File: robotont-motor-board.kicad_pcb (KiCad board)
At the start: 2 copper layers, 28 parts, among them J1 PWR_IN, J2 ENC, J3 MOTOR, J4 Conn_02x05_Odd_Even, U1 DMS3015SSS-13, U3 MIC5205-X.X

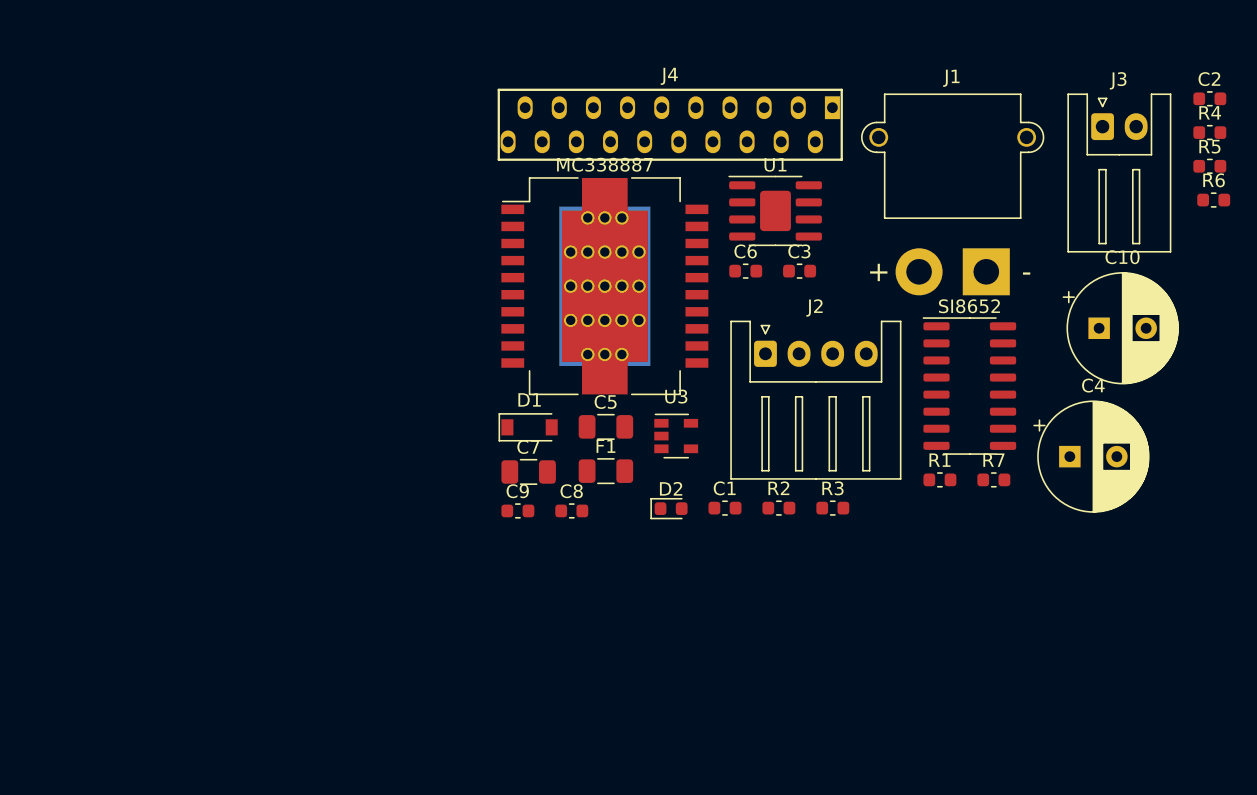
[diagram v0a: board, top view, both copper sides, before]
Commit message: v2.1 with jlcpcb components
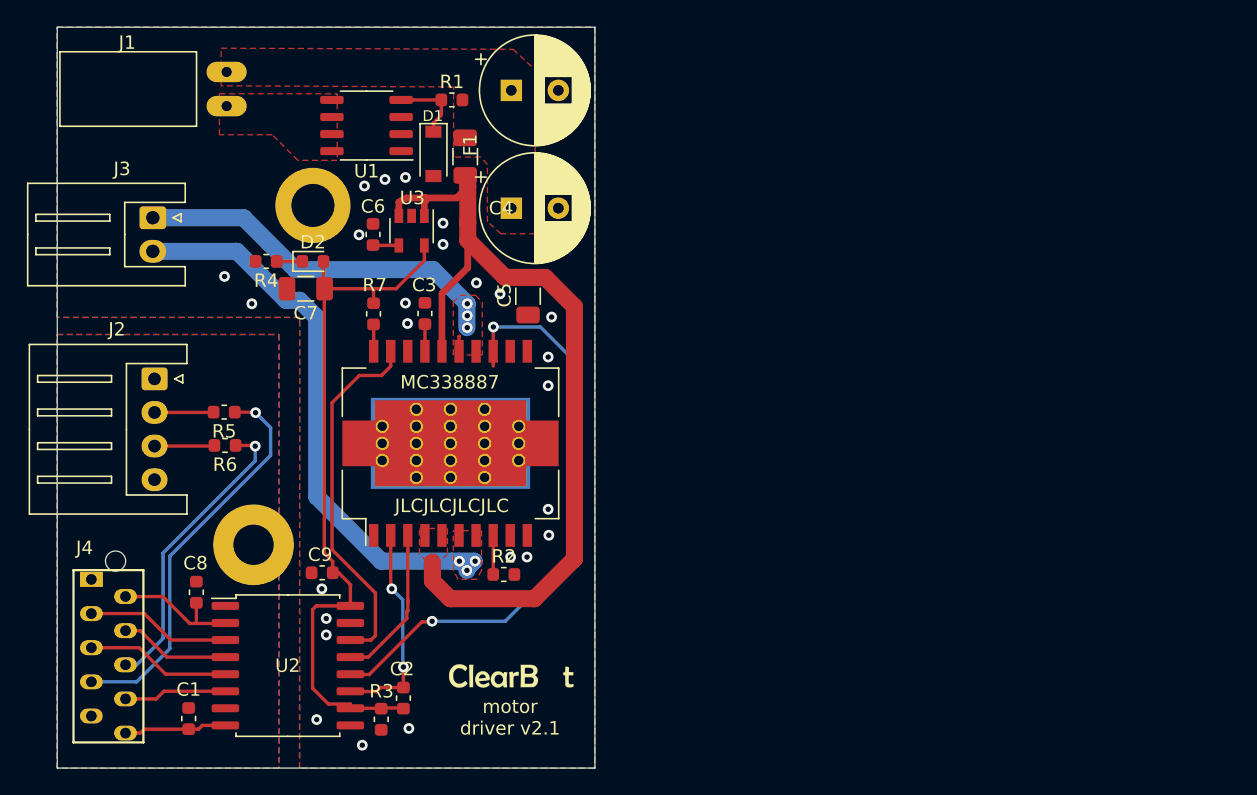
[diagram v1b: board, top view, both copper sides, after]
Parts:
- removed SI8652: SI8652-IS, Package_SO:SOIC-16_3.9x9.9mm_P1.27mm
- added G***: LOGO, robotont-motor-board:clearbot_logo, F.Cu at (134.4, 98.3)
- added H1: MountingHole_Pad, MountingHole:MountingHole_3mm_Pad, F.Cu at (115.2, 88.5)
- added H2: MountingHole_Pad, MountingHole:MountingHole_3.2mm_M3_DIN965_Pad, F.Cu at (119.6, 63.3)
- added U2: Si8641BD-B-IS, Package_SO:SOIC-16W_7.5x10.3mm_P1.27mm, F.Cu at (117.7, 97.5)
- J1: footprint Connector_AMASS:AMASS_XT30PW-M_1x02_P2.50mm_Horizontal -> robotont-motor-board:KF2510-2AWG
- J4: footprint footprints:CONN-TE-MICROMATCH-10X2-PTH -> footprints:CONN-TE-MICROMATCH-5X2-PTH-BOSS
- U1: value DMS3015SSS-13 -> NTMS4807N; footprint Package_SO:SOIC-8-1EP_3.9x4.9mm_P1.27mm_EP2.29x3mm -> Package_SO:SO-8_3.9x4.9mm_P1.27mm
- moved C2 77.0 mm to (124.7, 101.5), turned to 270 degrees
- moved R6 75.8 mm to (113.1, 81.2), turned to 180 degrees
- moved R5 75.6 mm to (113.0, 78.7), turned to 180 degrees
- moved J3 71.0 mm to (107.7, 64.2), turned to 270 degrees
- moved R4 70.9 mm to (116.1, 67.5), turned to 180 degrees
- moved J1 70.8 mm to (100.8, 51.9)
- moved J4 57.5 mm to (104.4, 96.8), turned to 90 degrees
- moved R7 47.8 mm to (124.1, 71.4), turned to 270 degrees
- moved C10 47.2 mm to (134.4, 54.7)
- moved R1 46.0 mm to (129.9, 55.4), turned to 180 degrees
- moved J2 45.5 mm to (107.8, 76.2), turned to 270 degrees
- moved C4 45.5 mm to (134.4, 63.5)
- moved C1 42.9 mm to (110.4, 101.5), turned to 270 degrees
- moved R3 34.9 mm to (126.3, 99.9), turned to 90 degrees
- moved D2 32.4 mm to (119.6, 67.5)
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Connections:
- net Net-(MC338887-Pad2) renamed /FAULT_D
- net Net-(MC338887-Pad8) renamed /FB_D
- J1 pad 1: GNDA_IN -> VCC_IN
- J1 pad 2: VCC_IN -> GNDA_IN
- J2 pad 1: +3V3 -> GND
- J2 pad 4: GND -> +3V3
- J3 pad 1: MOTOR1 -> MOTOR2
- J3 pad 2: MOTOR2 -> MOTOR1
- J4 pad 9: FB -> GND
- MC338887 pad 21: (no net) -> GNDA
- R5 pad 2: Net-(J2-Pad3) -> Net-(J2-Pad2)
- R6 pad 2: Net-(J2-Pad2) -> Net-(J2-Pad3)
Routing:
- net VCC: track 0.00 -> 67.7 mm
- net +5V: track 0.00 -> 53.3 mm
- net PWM_D: track 0.00 -> 44.4 mm, vias 0 -> 2
- net MOTOR1: track 0.00 -> 42.2 mm, vias 0 -> 3
- net ENCB: track 0.00 -> 29.5 mm, vias 0 -> 1
- net MOTOR2: track 0.00 -> 29.0 mm, vias 0 -> 3
- net DIR2_D: track 0.00 -> 27.3 mm
- net ENCA: track 0.00 -> 22.3 mm, vias 0 -> 1
- net GND: track 0.00 -> 17.1 mm
- net /FAULT_D: track 0.00 -> 15.7 mm, vias 0 -> 2
- net DIR1_D: track 0.00 -> 11.9 mm
- net PWM: track 0.00 -> 10.8 mm
- net DIR2: track 0.00 -> 10.8 mm
- net DIR1: track 0.00 -> 8.24 mm
- net FAULT: track 0.00 -> 7.67 mm
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- added copper zone on F.Cu, net +3V3
- added copper zone on B.Cu, net GND
- added copper zone on B.Cu, net GNDA
- added copper zone on F.Cu, net GNDA
- added copper zone on F.Cu, net GNDA_IN
- added copper zone on F.Cu, net MOTOR1
- added copper zone on F.Cu, net MOTOR2
- added copper zone on F.Cu, net VCC
- added copper zone on F.Cu, net VCC_IN
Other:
- board outline added: 40 x 55.1 mm
- net class motor added: clearance 0.4, trace_width 1.5, via_dia 0.8, via_drill 0.4
- board text added: "JLCJLCJLCJLC"
- board text added: "motor driver v2.1"
